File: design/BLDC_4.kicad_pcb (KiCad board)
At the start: 4 copper layers, 38.5 x 65 mm, 127 parts, among them K1 SERVO, P1 HALL/Encoder, P101 CANBUS, P2 SWD, P3 PWR_COMM, P4 IN+, P5 IN-, P6 MOTOR1, P7 MOTOR2, P9 MOTOR3, Q1 IRFS7530, Q2 IRFS7530, Q3 IRFS7530, Q4 IRFS7530, Q5 IRFS7530, Q6 IRFS7530, U1 STM32F40X_LQFP64, U2 TC2117, U3 DRV8302, U401 SN65HVD232, X1 MINI-USB-SHIELD-32005-201, X2 8MHz 10ppm

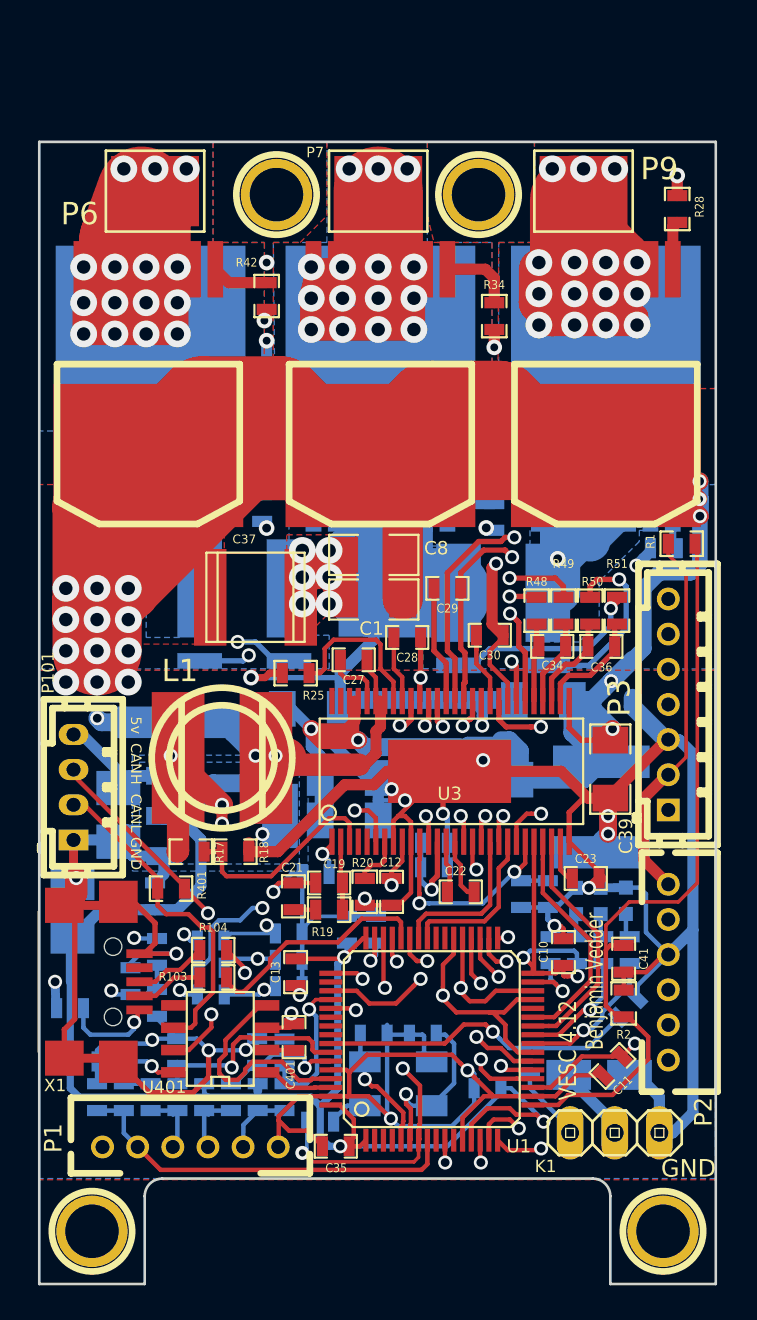
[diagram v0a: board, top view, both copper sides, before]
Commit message: Addition of board mount headers and vertical USB connectors
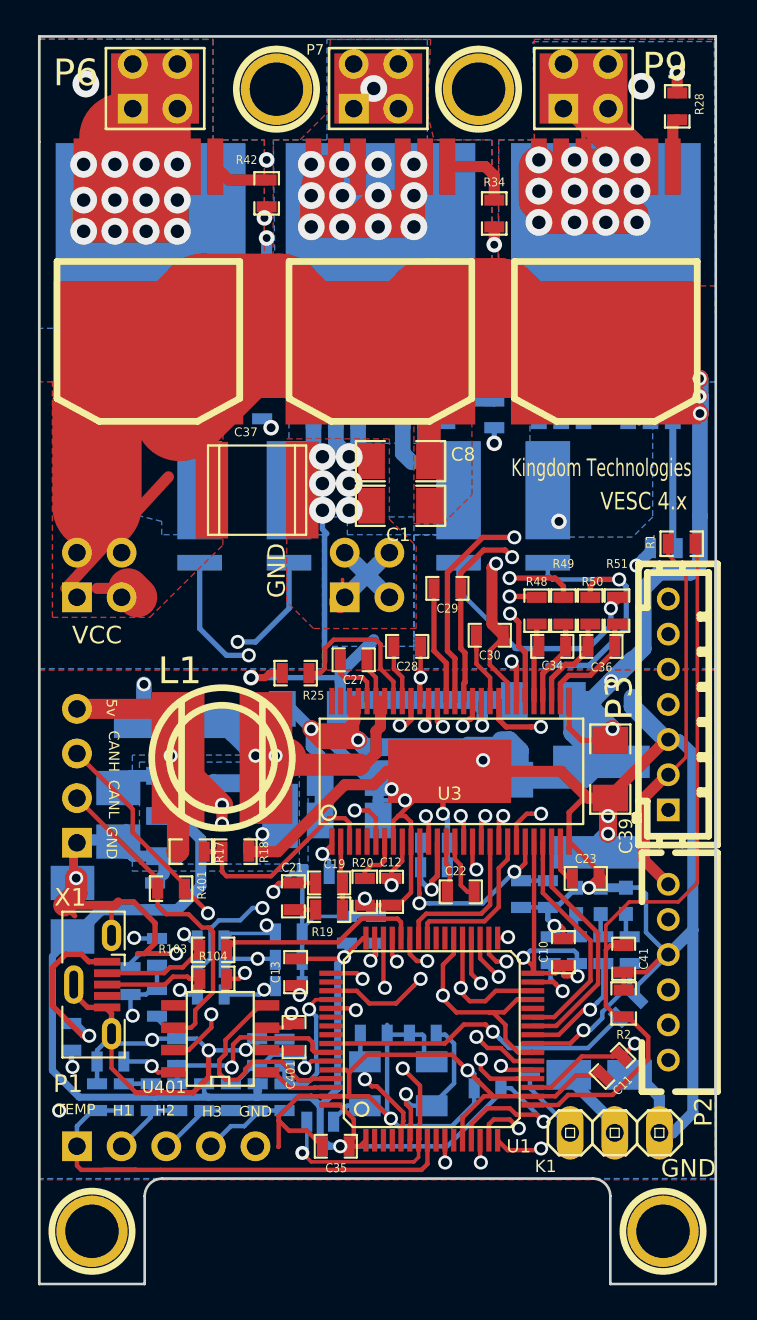
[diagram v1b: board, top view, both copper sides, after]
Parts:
- removed the 1PIN at (92.0, 83.0)
- removed the 1PIN at (103.5, 83.0)
- removed P101: CANBUS, JST conn:b4b-ph-kl
- removed P4: IN+, CRF1:1PAD_4x5mm
- removed P5: IN-, CRF1:1PAD_4x5mm
- added 1PIN: P***, 1pin, F.Cu at (92.0, 77.0)
- added 1PIN: P***, 1pin, F.Cu at (103.5, 77.0)
- added J1: VCC_IN, Connector_PinHeader_2.54mm:PinHeader_2x02_P2.54mm_Vertical, B.Cu at (80.6, 105.9)
- added J2: GND_IN, Connector_PinHeader_2.54mm:PinHeader_2x02_P2.54mm_Vertical, B.Cu at (95.9, 105.9)
- added REF**: PinHeader_1x04_P2.54mm_Vertical, Connector_PinHeader_2.54mm:PinHeader_1x04_P2.54mm_Vertical, B.Cu at (80.6, 119.9)
- added REF**: PinHeader_2x02_P2.54mm_Vertical, Connector_PinHeader_2.54mm:PinHeader_2x02_P2.54mm_Vertical, B.Cu at (108.3, 78.1)
- added REF**: PinHeader_2x02_P2.54mm_Vertical, Connector_PinHeader_2.54mm:PinHeader_2x02_P2.54mm_Vertical, B.Cu at (83.8, 78.1)
- added REF**: PinHeader_2x02_P2.54mm_Vertical, Connector_PinHeader_2.54mm:PinHeader_2x02_P2.54mm_Vertical, B.Cu at (96.4, 78.1)
- P1: value HALL/Encoder -> PinHeader_1x05_P2.54mm_Vertical; footprint CRF1:MICRO_JST_6 -> Connector_PinHeader_2.54mm:PinHeader_1x05_P2.54mm_Vertical; moved to B.Cu
- X1: value MINI-USB-SHIELD-32005-201 -> USB_Micro-B_Molex-105133-0001; footprint CRF1:USB-UX60R-MB-5ST -> Connector_USB:USB_Micro-B_Molex-105133-0001
- moved G*** 15.0 mm to (113.9, 98.6)
- moved P1 6.46 mm to (80.6, 137.2), turned to 270 degrees
- moved C37 6.10 mm to (90.9, 99.8)
- moved P6 5.84 mm to (85.1, 77.0)
- moved P7 5.84 mm to (97.8, 77.0)
- moved P9 5.84 mm to (109.5, 77.0)
- moved Q1 5.84 mm to (110.7, 86.1)
- moved Q2 5.84 mm to (110.7, 90.0)
- moved Q3 5.84 mm to (97.9, 86.1)
- moved Q4 5.84 mm to (97.9, 90.0)
- moved Q5 5.84 mm to (84.7, 86.1)
- moved Q6 5.84 mm to (84.8, 90.0)
- moved R28 5.84 mm to (114.8, 78.0)
- moved R30 5.84 mm to (104.4, 90.3)
- moved R34 5.84 mm to (104.4, 84.1)
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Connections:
- P1 pad 1: +5V -> /Filters/TEMP_IN
- P1 pad 2: /Filters/TEMP_IN -> /Filters/HALL1_IN
- P1 pad 3: /Filters/HALL1_IN -> /Filters/HALL2_IN
- P1 pad 4: /Filters/HALL2_IN -> /Filters/HALL3_IN
- P1 pad 5: /Filters/HALL3_IN -> GND
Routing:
- net GND: track 398.8 -> 374.3 mm
- net V_SUPPLY: track 290.3 -> 308.5 mm, vias 20 -> 8
- net /Mosfet driver/H1_LOW: track 48.5 -> 37.0 mm
- net /Mosfet driver/M_L3: track 20.0 -> 28.6 mm
- net /Filters/TEMP_IN: track 22.4 -> 28.7 mm
- net /Mosfet driver/M_H1: track 49.8 -> 55.6 mm
- net Net-(Q2-PadG): track 16.2 -> 22.0 mm
- net /Mosfet driver/M_H2: track 24.4 -> 30.3 mm
- net /Mosfet driver/M_H3: track 40.9 -> 46.7 mm
- net /Mosfet driver/SH2_A: track 10.7 -> 15.6 mm
- net Net-(R6-Pad1): track 5.50 -> 9.88 mm
- net /Mosfet driver/H3_LOW: track 53.5 -> 57.0 mm
- net /Mosfet driver/M_L2: track 19.3 -> 22.5 mm
- net /Mosfet driver/SH2_B: track 11.4 -> 14.5 mm
- net /Mosfet driver/SH1_B: track 25.0 -> 27.2 mm
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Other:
- board size 38.5 x 65 mm -> 38.5 x 71 mm
- board text added: "Kingdom Technologies"
- board text added: "VCC"
- board text added: "VESC 4.x"
- board text removed: "Benjamin Vedder"
- board text removed: "VESC 4.12"
- board text removed: "vedder.se"

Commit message: Cleared out files, updated gerbers, added BOM
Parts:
- removed REF** (x2): PinHeader_2x02_P2.54mm_Vertical, Connector_PinHeader_2.54mm:PinHeader_2x02_P2.54mm_Vertical
- added J3: PinHeader_2x02_P2.54mm_Vertical, Connector_PinHeader_2.54mm:PinHeader_2x02_P2.54mm_Vertical, B.Cu at (83.8, 78.1)
- added J5: PinHeader_2x02_P2.54mm_Vertical, Connector_PinHeader_2.54mm:PinHeader_2x02_P2.54mm_Vertical, B.Cu at (108.3, 78.1)
- renumbered REF** to J4, REF** to P3
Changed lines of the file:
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@@
   (layers
     (0 F.Cu signal)
-    (1 GND signal hide)
-    (2 GND2 signal hide)
-    (31 B.Cu signal hide)
-    (32 B.Adhes user hide)
-    (33 F.Adhes user hide)
-    (34 B.Paste user hide)
-    (35 F.Paste user hide)
+    (1 GND signal)
+    (2 GND2 signal)
+    (31 B.Cu signal)
+    (32 B.Adhes user)
+    (33 F.Adhes user)
+    (34 B.Paste user)
+    (35 F.Paste user)
     (36 B.SilkS user)
     (37 F.SilkS user)
@@
   )
   (setup
-    (last_trace_width 0.889)
+    (last_trace_width 0.2032)
     (user_trace_width 0.254)
     (user_trace_width 0.3048)
@@
     (visible_elements 7FFFFFFF)
     (pcbplotparams
-      (layerselection 0x010fc_80000007)
+      (layerselection 0x010fc_ffffffff)
       (usegerberextensions true)
       (usegerberattributes false)
@@
     (descr "Through hole straight pin header, 1x04, 2.54mm pitch, single row")
     (tags "Through hole pin header THT 1x04 2.54mm single row")
-    (fp_text reference REF** (at 0 2.33) (layer B.SilkS)
+    (fp_text reference P3 (at 0 2.33) (layer B.SilkS)
       (effects (font (size 1 1) (thickness 0.15)) (justify mirror))
     )
@@
     (descr "Through hole straight pin header, 2x02, 2.54mm pitch, double rows")
     (tags "Through hole pin header THT 2x02 2.54mm double row")
-    (fp_text reference REF** (at 1.27 2.33) (layer B.SilkS)
+    (fp_text reference J5 (at 1.27 2.33) (layer B.SilkS)
       (effects (font (size 1 1) (thickness 0.15)) (justify mirror))
     )
@@
     (descr "Through hole straight pin header, 2x02, 2.54mm pitch, double rows")
     (tags "Through hole pin header THT 2x02 2.54mm double row")
-    (fp_text reference REF** (at 1.27 2.33) (layer B.SilkS)
+    (fp_text reference J3 (at 1.27 2.33) (layer B.SilkS)
       (effects (font (size 1 1) (thickness 0.15)) (justify mirror))
     )
@@
     (descr "Through hole straight pin header, 2x02, 2.54mm pitch, double rows")
     (tags "Through hole pin header THT 2x02 2.54mm double row")
-    (fp_text reference REF** (at 1.27 2.33) (layer B.SilkS)
+    (fp_text reference J4 (at 1.27 2.33) (layer B.SilkS)
       (effects (font (size 1 1) (thickness 0.15)) (justify mirror))
     )
@@
   )
   (gr_line (start 117 74) (end 78.5 74) (angle 90) (layer Edge.Cuts) (width 0.15))
-  (via (at 81.3435 130.8735) (size 0.8) (drill 0.5) (layers F.Cu B.Cu) (net 37))
   (via (at 79.629 135.128) (size 0.8) (drill 0.5) (layers F.Cu B.Cu) (net 1))
   (segment (start 114.3 118.03126) (end 114.3 119.634) (width 1.016) (layer GND) (net 1) (status 1000010))
@@
   (segment (start 94.488 110.236) (end 93.853 110.236) (width 0.254) (layer F.Cu) (net 36) (status 20))
   (segment (start 98.65614 111.8235) (end 98.65614 110.72114) (width 0.254) (layer F.Cu) (net 36) (status 10))
+  (via (at 81.3435 130.8735) (size 0.8) (drill 0.5) (layers F.Cu B.Cu) (net 37))
   (segment (start 80.645 130.175) (end 81.3435 130.8735) (width 0.3048) (layer B.Cu) (net 37))
   (segment (start 80.3275 130.175) (end 80.645 130.175) (width 0.3048) (layer B.Cu) (net 37))
